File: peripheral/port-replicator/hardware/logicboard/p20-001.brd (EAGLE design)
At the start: 72 x 72 mm, 8 parts, among them J1 DIN5, J2 DIN5, J3 DIN5

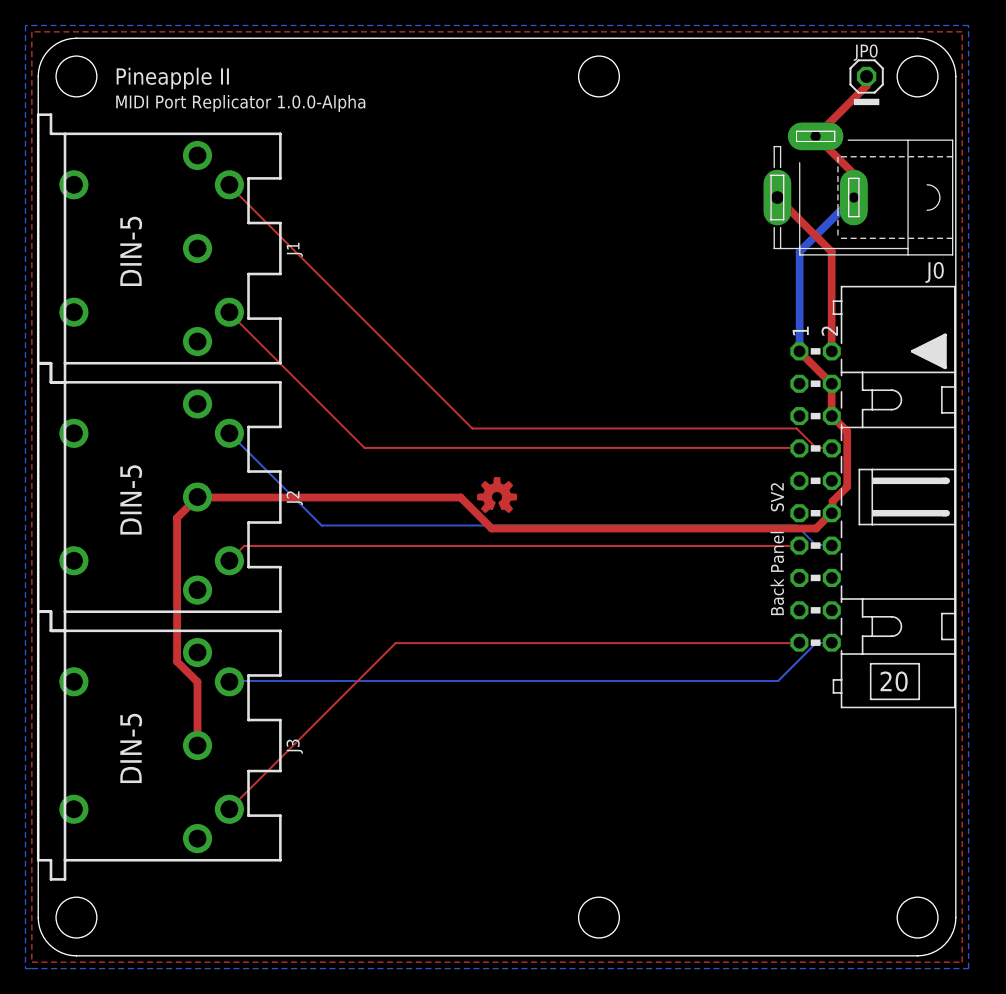
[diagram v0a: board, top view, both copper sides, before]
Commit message: Remake of port rep.
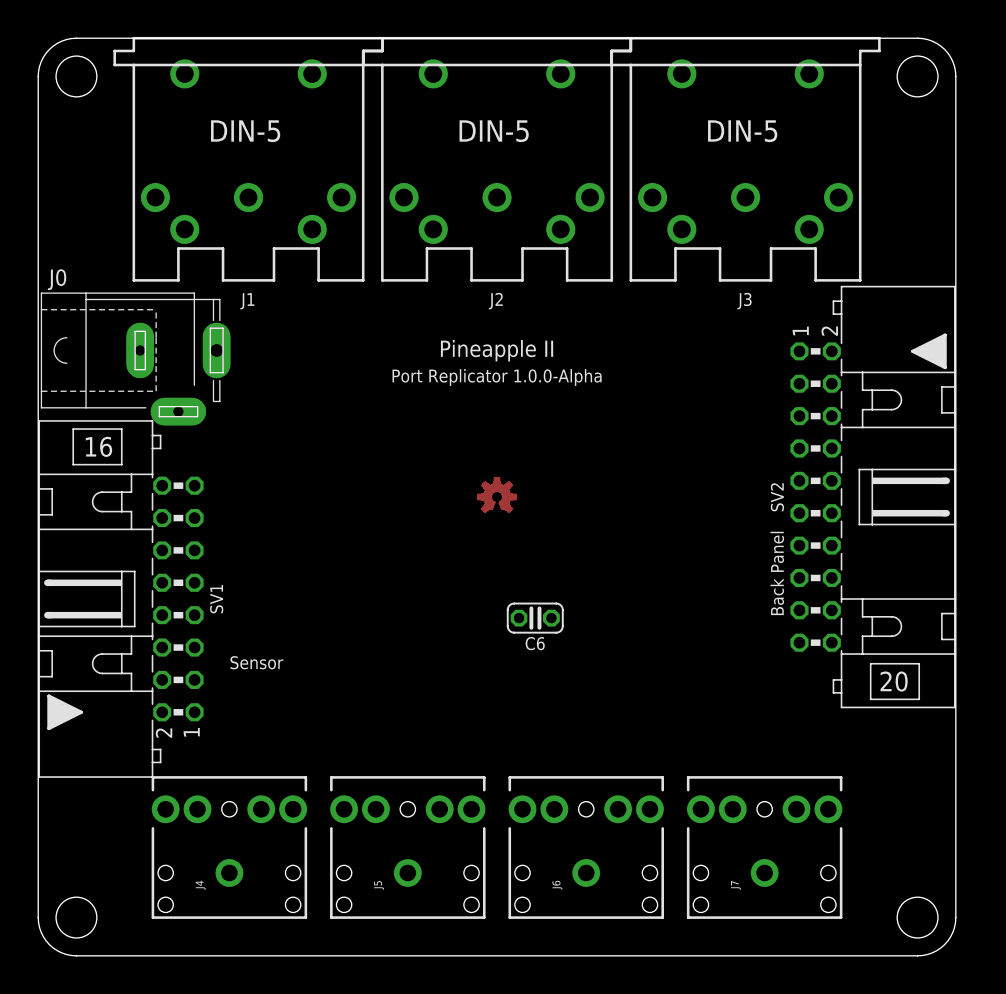
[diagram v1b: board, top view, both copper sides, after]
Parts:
- removed JP0: GNDPIN, pinhead:1X01
- added C6: 10n, resistor:C025-024X044
- added J4, J5, J6, J7: AUDIO_JACK_3.5MM_PTH, SparkFun-Connectors:AUDIO-JACK
- added SV1: (no value), con-ml:ML16L
- moved J3 78.5 mm to (55.5, 72.0), turned to 180 degrees
- moved J0 51.4 mm to (11.0, 47.5), turned to 0 degrees
- moved J2 50.9 mm to (36.0, 72.0), turned to 180 degrees
- moved J1 23.3 mm to (16.5, 72.0), turned to 180 degrees
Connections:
- net MO2RETN renamed MTRTN
- net MO2SEND renamed MTSND
- removed net MIRETN: J1.5, SV2.8
- removed net MISEND: J1.4, SV2.7
- removed net MO1RETN: J2.5, SV2.14
- removed net MO1SEND: J2.4, SV2.13
- removed net MTRETN: J3.5, SV2.20
- removed net MTSEND: J3.4, SV2.19
- new net ANLG1R: SV1.4
- new net ANLG2R: SV1.8
- new net ANLG3R: SV1.12
- new net ANLG4R: SV1.16
- new net DTCT1: SV1.3
- new net DTCT2: SV1.7
- new net DTCT3: SV1.11
- new net DTCT4: SV1.15
- new net MIRTN: SV2.8
- new net MISND: SV2.7
- new net MORTN: SV2.14
- new net MOSND: SV2.13
- new net VCC: C6.1, SV2.19
- new net VCC/2: SV1.10, SV1.14, SV1.2, SV1.6
- net GND: now also C6.2, SV1.1, SV1.13, SV1.5, SV1.9, SV2.20; no longer J0.1, J0.2, J2.2, J3.2, JP0.1
- net V+: no longer J0.3
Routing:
- net GND: track 113.2 -> 0.00 mm
- net MIRETN: track 55.9 -> 0.00 mm
- net MO1RETN: track 50.9 -> 0.00 mm
- net MTSEND: track 50.1 -> 0.00 mm
- net MISEND: track 49.2 -> 0.00 mm
- net MTRETN: track 48.6 -> 0.00 mm
- net MO1SEND: track 45.2 -> 0.00 mm
- net V+: track 13.8 -> 0.00 mm
- removed copper zone on layer 1, net GND
- removed copper zone on layer 16, net GND
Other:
- board text added: "Port Replicator 1.0.0-Alpha"
- board text added: "Sensor"
- board text removed: "MIDI IN"
- board text removed: "MIDI OUT"
- board text removed: "MIDI Port Replicator 1.0.0-Alpha"
- board text removed: "MIDI THRU"

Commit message: Hmm...
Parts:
- removed J5, J6, J7: AUDIO_JACK_3.5MM_PTH, SparkFun-Connectors:AUDIO-JACK
- added J11, J12, J13: DIN5, SparkFun-Connectors:DIN5-RA-PTH
- J1, J2, J3: value DIN5 -> AUDIO_JACK_3.5MM_PTH; device SparkFun-Connectors:DIN5-RA-PTH -> SparkFun-Connectors:AUDIO-JACK
- moved J3 66.7 mm to (43.0, 6.50), turned to 90 degrees
- moved J2 65.9 mm to (29.0, 6.50), turned to 90 degrees
- moved J1 65.5 mm to (15.0, 6.50), turned to 90 degrees
- moved J4 42.0 mm to (57.0, 6.50)
- renumbered C6 to C1
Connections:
- net GND: now also J0.1, J0.2, J12.2, J13.2
- net MIRTN: now also J11.5
- net MISND: now also J11.4
- net MORTN: now also J13.5
- net MOSND: now also J13.4
- net MTRTN: now also J12.5
- net MTSND: now also J12.4
- net V+: now also J0.3
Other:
- board text added: "IN"
- board text added: "OUT"
- board text added: "THRU"
- board text removed: "Back Panel"
- board text removed: "Sensor"

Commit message: Trying to implement a port replicator.
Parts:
- added JP1: (no value), adafruit:2X04
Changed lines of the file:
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@@
 <attribute name="VALUE" x="59.667" y="5.23" size="0.6096" layer="27" font="vector" ratio="20" rot="R90"/>
+</element>
+<element name="JP1" library="adafruit" library_urn="urn:adsk.eagle:library:420" package="2X04" package3d_urn="urn:adsk.eagle:package:6240893/1" value="" x="67" y="11.5" smashed="yes" rot="R90">
+<attribute name="NAME" x="63.825" y="6.42" size="1.27" layer="25" ratio="10" rot="R90"/>
+<attribute name="VALUE" x="71.445" y="6.42" size="1.27" layer="27" rot="R90"/>
 </element>
 </elements>

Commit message: Initial layout.
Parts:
- added IC1: 74LS07N, 74xx-us:DIL14
- added LED1, LED2, LED3: (no value), led:LED3MM
- added R1, R2, R3: (no value), rcl:0204/5
- moved C1 4.61 mm to (36.0, 30.0)
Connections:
- new net ANGL4R: J4.RING
- new net N$1: IC1.2, R2.1
- new net N$2: IC1.4, R3.1
- new net N$3: LED2.K, R2.2
- new net N$4: LED3.K, R3.2
- net ANLG1R: now also J1.RING
- net ANLG2R: now also J2.RING
- net ANLG3R: now also J3.RING
- net DTCT1: now also JP1.1
- net DTCT2: now also JP1.3
- net DTCT3: now also JP1.5
- net DTCT4: now also JP1.7
- net GND: now also IC1.11, IC1.13, IC1.5, IC1.7, IC1.9, J1.SLEEVE, J2.SLEEVE, J3.SLEEVE, J4.SLEEVE, JP1.2, JP1.4, JP1.6, JP1.8
- net MIRTN: now also IC1.1
- net MOSND: now also IC1.3
- net VCC: now also IC1.14, LED2.A, LED3.A
- net VCC/2: now also J1.TIP, J2.TIP, J3.TIP, J4.TIP
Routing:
- net GND: track 0.00 -> 234.6 mm
- net MIRTN: track 0.00 -> 108.7 mm
- net VCC: track 0.00 -> 89.2 mm
- net VCC/2: track 0.00 -> 81.6 mm
- net DTCT4: track 0.00 -> 66.9 mm
- net DTCT3: track 0.00 -> 64.7 mm
- net DTCT2: track 0.00 -> 63.7 mm
- net MISND: track 0.00 -> 63.5 mm
- net DTCT1: track 0.00 -> 62.0 mm
- net V+: track 0.00 -> 59.6 mm
- net MOSND: track 0.00 -> 58.8 mm, vias 0 -> 1
- net MTSND: track 0.00 -> 50.1 mm
- net N$3: track 0.00 -> 46.6 mm
- net MTRTN: track 0.00 -> 41.8 mm
- net N$4: track 0.00 -> 41.5 mm
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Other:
- board text added: "DC9-12V"

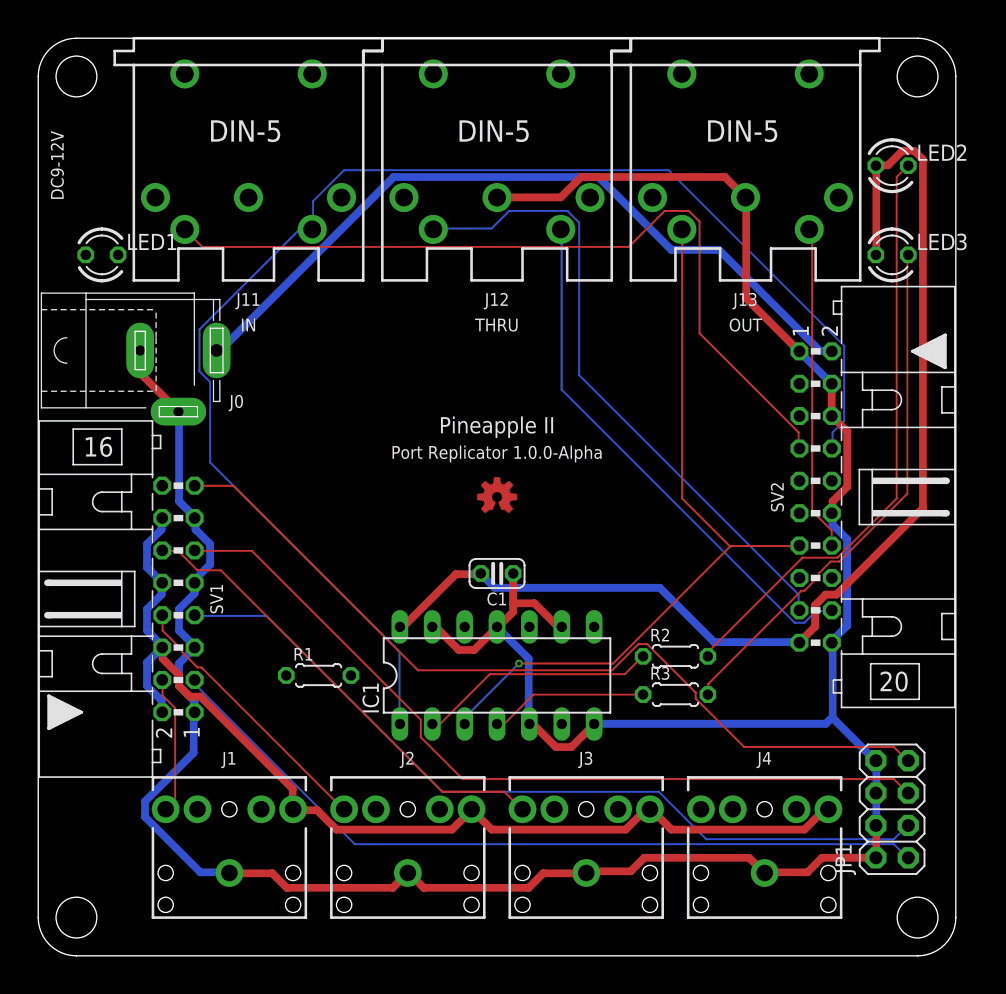
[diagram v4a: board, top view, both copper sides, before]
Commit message: Design of the port replicator.
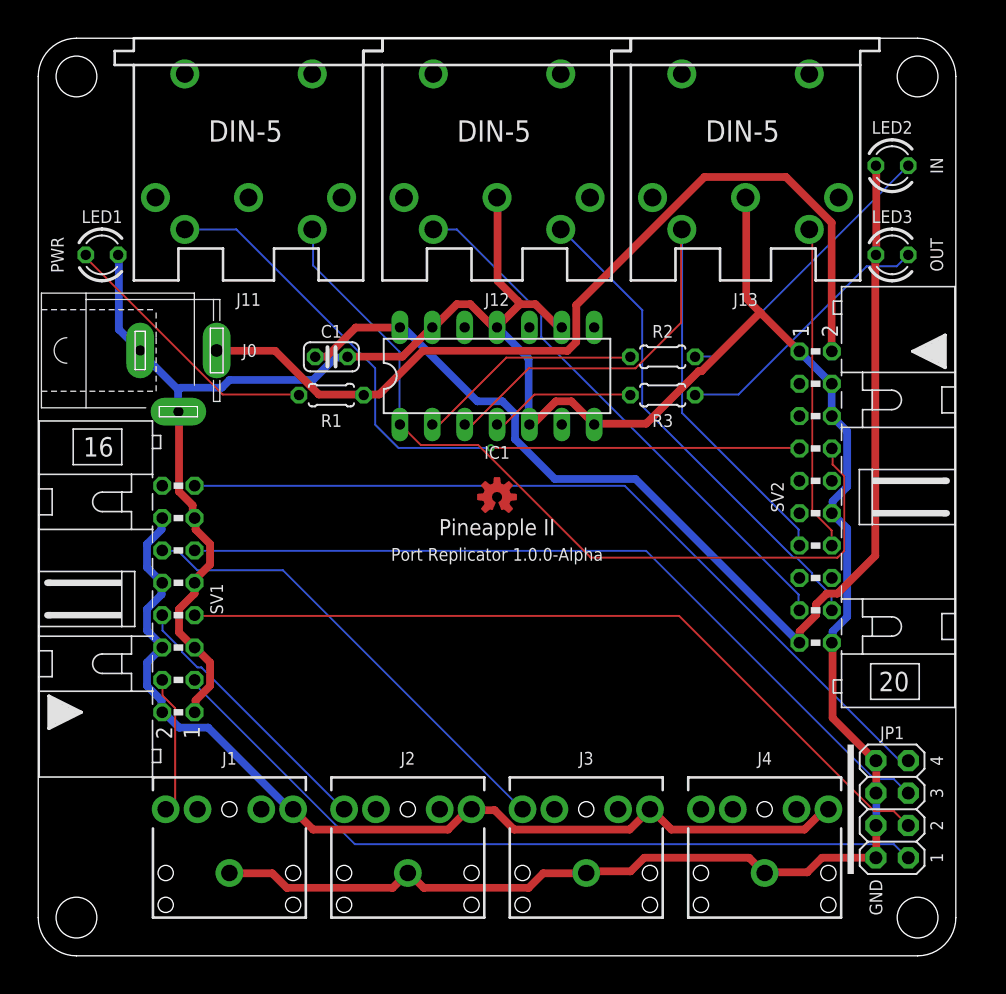
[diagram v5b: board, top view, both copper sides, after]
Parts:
- moved R2 23.5 mm to (49.0, 47.0)
- moved R3 23.5 mm to (49.0, 44.0)
- moved IC1 23.5 mm to (36.0, 45.5)
- moved R1 22.0 mm to (23.0, 44.0)
- moved C1 21.4 mm to (23.0, 47.0)
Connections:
- net N$3 renamed MILED
- net N$4 renamed MOLED
- new net N$4: LED1.A, R1.1
- net GND: now also LED1.K
- net V+: now also R1.2
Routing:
- net MIRTN: track 108.7 -> 66.1 mm
- net MILED: track 46.6 -> 22.9 mm
- net N$4: track 0.00 -> 21.4 mm
- net MOLED: track 41.5 -> 21.3 mm
- net V+: track 59.6 -> 70.1 mm
- net MTSND: track 50.1 -> 42.9 mm
- net MISND: track 63.5 -> 57.9 mm, vias 0 -> 1
- net GND: track 234.6 -> 229.9 mm
- net VCC/2: track 81.6 -> 77.6 mm
- net MTRTN: track 41.8 -> 38.9 mm
- net MOSND: track 58.8 -> 56.3 mm, vias 1 -> 0
- net DTCT4: track 66.9 -> 64.9 mm
- net VCC: track 89.2 -> 90.8 mm
- net N$1: track 18.7 -> 17.8 mm
- net N$2: track 12.4 -> 11.5 mm
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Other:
- board text added: "1"
- board text added: "2"
- board text added: "3"
- board text added: "4"
- board text added: "GND"
- board text added: "MIDI"
- board text added: "PWR"
- board text added: "Tip: DC5V, Ring: Sensor, Sleeve: GND"

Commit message: Port replicator.
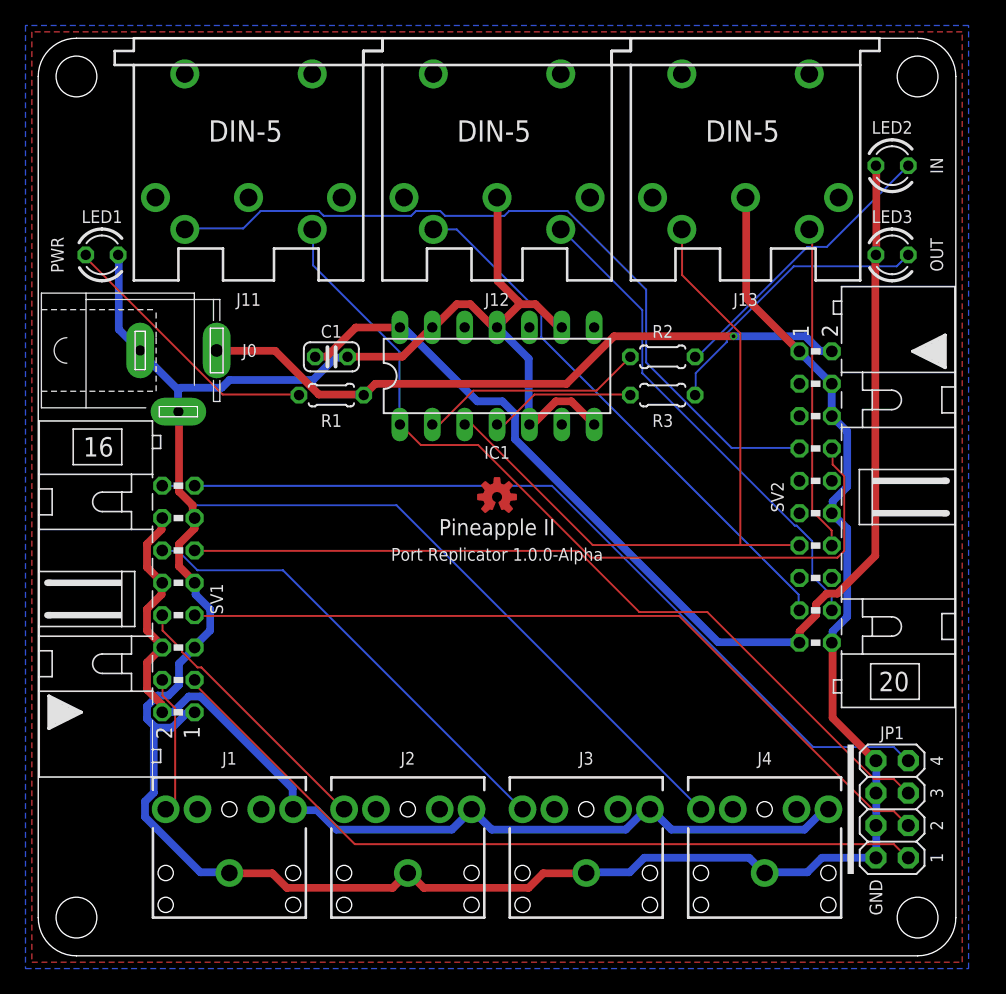
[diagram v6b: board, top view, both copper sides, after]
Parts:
- J0: value (none) -> DC9V
- LED1: value (none) -> PWR
- LED2: value (none) -> IN
- LED3: value (none) -> OUT
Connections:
- removed net ANGL4R: J4.RING
- net ANLG4R: now also J4.RING
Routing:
- net ANLG4R: track 0.00 -> 52.8 mm
- net V+: track 70.1 -> 52.1 mm, vias 0 -> 1
- net GND: track 229.9 -> 235.1 mm
- net MISND: track 57.9 -> 60.6 mm, vias 1 -> 0
- net VCC/2: track 77.6 -> 79.6 mm
- net MOLED: track 21.3 -> 22.7 mm
- net MOSND: track 56.3 -> 56.9 mm
- added copper zone on layer 1, net GND
- added copper zone on layer 16, net GND
